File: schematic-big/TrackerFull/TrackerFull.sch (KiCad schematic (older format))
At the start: 50 parts, among them J1 SIM_Card, J2 Conn_01x05_Male, J7 Screw_Terminal_01x02, J8 USB_B_Mini, Q1 IRLML5203, Q2 IRLML0030, Q3 IRLML0030, U1 U.FL, U2 LIS3DSH, U3 MCP73831-2-OT, U4 LM350_TO220, U6 ATtiny85-20SU, U7 MCP1700-2502E_SOT23

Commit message: schematic fixes
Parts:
- R10, R11, R9: value 140 -> 125
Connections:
- wire segments 205 -> 203
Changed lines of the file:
@@
 P 2700 6150
 F 0 "R11" V 2630 6104 50  0000 R CNN
-F 1 "140" V 2600 6400 50  0000 R CNN
+F 1 "125" V 2600 6400 50  0000 R CNN
 F 2 "Resistor_SMD:R_0805_2012Metric_Pad1.15x1.40mm_HandSolder" H 2630 6241 50  0001 R CNN
 F 3 "~" H 2700 6150 50  0001 C CNN
@@
 P 2650 6350
 F 0 "R10" V 2580 6304 50  0000 R CNN
-F 1 "140" V 2550 6600 50  0000 R CNN
+F 1 "125" V 2550 6600 50  0000 R CNN
 F 2 "Resistor_SMD:R_0805_2012Metric_Pad1.15x1.40mm_HandSolder" H 2580 6441 50  0001 R CNN
 F 3 "~" H 2650 6350 50  0001 C CNN
@@
 P 2600 6550
 F 0 "R9" V 2530 6504 50  0000 R CNN
-F 1 "140" V 2450 6800 50  0000 R CNN
+F 1 "125" V 2450 6800 50  0000 R CNN
 F 2 "Resistor_SMD:R_0805_2012Metric_Pad1.15x1.40mm_HandSolder" H 2530 6641 50  0001 R CNN
 F 3 "~" H 2600 6550 50  0001 C CNN
@@
 Wire Wire Line
 	3050 6250 3450 6250
-Wire Wire Line
-	2950 6900 1800 6900
-Wire Wire Line
-	1800 6900 1800 6350
-Wire Wire Line
-	1800 6350 1950 6350
 $Comp
 L Regulator_Linear:MCP1700-2502E_SOT23 U7
@@
 Wire Wire Line
 	7600 5950 7750 5950
-Text Label 7850 5950 0    50   ~ 0
-2.2V
 Text Label 7000 7000 0    50   ~ 0
 2.2V
@@
 Wire Wire Line
 	6900 5950 7000 5950
-$Comp
-L Device:C C4
-U 1 1 5F5A6A6D
-P 7750 6100
-F 0 "C4" H 7865 6146 50  0000 L CNN
-F 1 "10uF" H 7865 6055 50  0000 L CNN
-F 2 "Capacitor_Tantalum_SMD:CP_EIA-3216-18_Kemet-A" H 7788 5950 50  0001 C CNN
-F 3 "~" H 7750 6100 50  0001 C CNN
-	1    7750 6100
-	1    0    0    -1
-$EndComp
 Connection ~ 7750 5950
 Wire Wire Line
@@
 	1    0    0    -1
 $EndComp
-Connection ~ 2950 6900
 $Comp
 L Transistor_FET:IRLML0030 Q3
@@
 	1    0    0    -1
 $EndComp
+$Comp
+L Device:C C4
+U 1 1 5F5A6A6D
+P 7750 6100
+F 0 "C4" H 7865 6146 50  0000 L CNN
+F 1 "10uF" H 7865 6055 50  0000 L CNN
+F 2 "Capacitor_Tantalum_SMD:CP_EIA-3216-18_Kemet-A" H 7788 5950 50  0001 C CNN
+F 3 "~" H 7750 6100 50  0001 C CNN
+	1    7750 6100
+	1    0    0    -1
+$EndComp
+Wire Wire Line
+	1500 6350 1950 6350
+Text Label 1500 6350 0    50   ~ 0
+2.2V
+Text Label 7850 5950 0    50   ~ 0
+2.2V
 $EndSCHEMATC

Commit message: schematic update
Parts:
- removed C14: 1uF, Capacitor_Tantalum_SMD:CP_EIA-3216-18_Kemet-A, symbol Device:C
- removed C3, C4: 10uF, Capacitor_Tantalum_SMD:CP_EIA-3216-18_Kemet-A, symbol Device:C
- removed LED1: TO-5050BC-MRPBFGF, LED_SMD:LED_RGB_5050-6, symbol Device:LED_RGB
- removed Q3: IRLML0030, Package_TO_SOT_SMD:SOT-23, symbol Transistor_FET:IRLML0030
- removed R10, R11: 125, Resistor_SMD:R_0805_2012Metric_Pad1.15x1.40mm_HandSolder, symbol Device:R
- removed R12: 100K, Resistor_SMD:R_0603_1608Metric, symbol Device:R
- removed U4: LM350_TO220, Package_TO_SOT_THT:TO-220-3_Horizontal_TabDown, symbol Regulator_Linear:LM350_TO220
- removed U7: MCP1700-2502E_SOT23, Package_TO_SOT_SMD:SOT-23, symbol Regulator_Linear:MCP1700-2502E_SOT23
- added C15: 10uF, Capacitor_Tantalum_SMD:CP_EIA-3216-18_Kemet-A, symbol Device:C
- added C18: 10uF, Capacitor_SMD:C_1206_3216Metric_Pad1.42x1.75mm_HandSolder, symbol Device:C
- added C19: 22uF, Capacitor_Tantalum_SMD:CP_EIA-3216-18_Kemet-A, symbol Device:C
- added C20: 4.7u, Capacitor_SMD:C_1206_3216Metric_Pad1.42x1.75mm_HandSolder, symbol Device:C
- added D3: SK6812, LED_SMD:LED_SK6812_PLCC4_5.0x5.0mm_P3.2mm, symbol LED:SK6812
- added L2: SRR0604-3R3ML, Inductor_THT:L_Radial_D8.7mm_P5.00mm_Fastron_07HCP, symbol mailboxNotifier-eagle-import:INDUCTOR
- added R14: 10K, Resistor_SMD:R_0805_2012Metric_Pad1.15x1.40mm_HandSolder, symbol Device:R
- added U5: LP2985-3.3, Package_TO_SOT_SMD:SOT-23-5, symbol Regulator_Linear:LP2985-3.3
- C12: renamed from C11; footprint Capacitor_Tantalum_SMD:CP_EIA-3216-18_Kemet-A -> Capacitor_SMD:C_1206_3216Metric_Pad1.42x1.75mm_HandSolder
- C13: renamed from C12; footprint Capacitor_Tantalum_SMD:CP_EIA-3216-18_Kemet-A -> Capacitor_SMD:C_1206_3216Metric_Pad1.42x1.75mm_HandSolder
- C14: renamed from C13; footprint Capacitor_Tantalum_SMD:CP_EIA-3216-18_Kemet-A -> Capacitor_SMD:C_1206_3216Metric_Pad1.42x1.75mm_HandSolder
- C8: footprint Capacitor_Tantalum_SMD:CP_EIA-3216-18_Kemet-A -> Capacitor_SMD:C_1206_3216Metric_Pad1.42x1.75mm_HandSolder
- D2: footprint Package_SO:SOP-8_3.76x4.96mm_P1.27mm -> Package_SO:SOP-8_3.9x4.9mm_P1.27mm
- J1: footprint Connector_Card:microSIM_JAE_SF53S006VCBR2000 -> mailboxNotifier:SIM_SOCKET1
- R2: value 47000 -> 43000
- R9: value 125 -> 10000; footprint Resistor_SMD:R_0805_2012Metric_Pad1.15x1.40mm_HandSolder -> Resistor_SMD:R_0603_1608Metric
- renumbered C15 to C21
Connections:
- net labels added: ACCEL_INT2, IO8, IO9, LED_CTL
- net labels removed: 2.2V, GPS_CTRL
- wire segments 203 -> 201
- no-connect marks 5 -> 6
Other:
- moved on the sheet: D1, J2

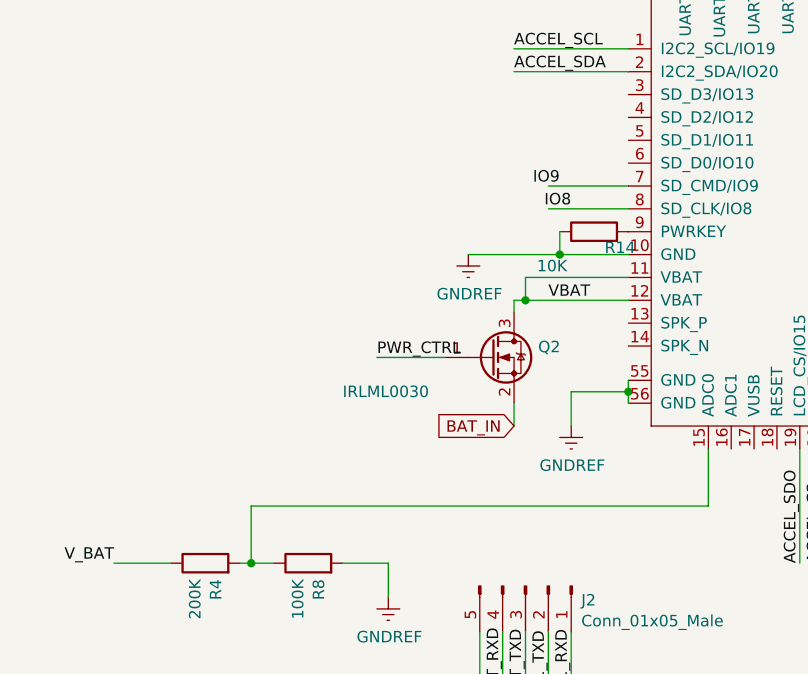
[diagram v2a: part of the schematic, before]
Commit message: schematic update
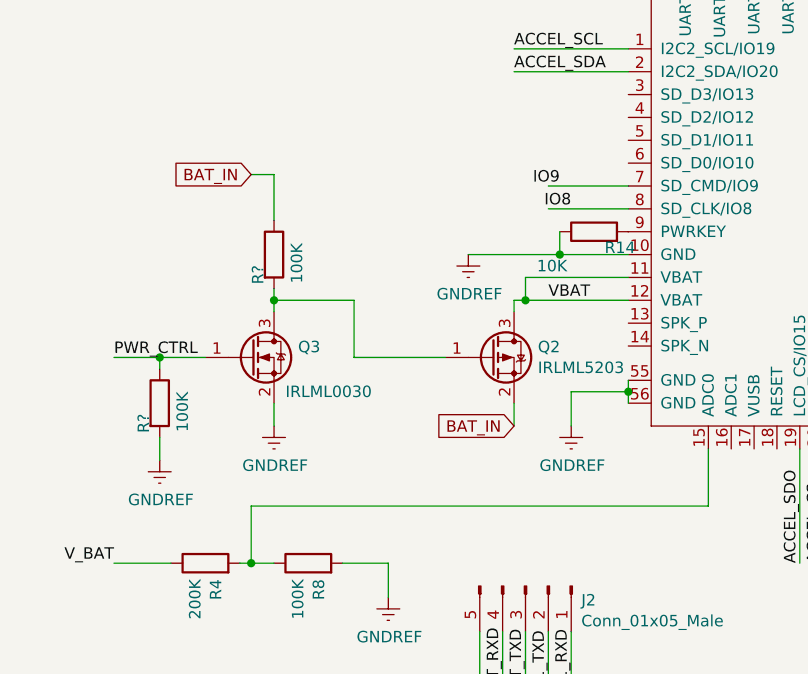
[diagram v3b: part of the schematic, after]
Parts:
- added Q2: IRLML5203, Package_TO_SOT_SMD:SOT-23, symbol Transistor_FET:IRLML5203
- added R? (x2): 100K, Resistor_SMD:R_0805_2012Metric_Pad1.15x1.40mm_HandSolder, symbol Device:R
- renumbered Q2 to Q3
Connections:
- wire segments 201 -> 212
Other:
- moved on the sheet: Q3
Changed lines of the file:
@@
 Wire Wire Line
 	2950 7300 2950 7400
-Text Label 2350 7100 0    50   ~ 0
+Text Label 1200 7100 0    50   ~ 0
 PWR_CTRL
 $Comp
@@
 	1    0    0    -1
 $EndComp
-Wire Wire Line
-	2350 7100 2650 7100
 Wire Wire Line
 	3000 6850 3450 6850
@@
 VBAT
 $Comp
-L Transistor_FET:IRLML0030 Q2
+L Transistor_FET:IRLML0030 Q3
 U 1 1 5F6E0FC1
-P 2850 7100
-F 0 "Q2" H 3055 7146 50  0000 L CNN
-F 1 "IRLML0030" H 2200 6950 50  0000 L CNN
-F 2 "Package_TO_SOT_SMD:SOT-23" H 3050 7025 50  0001 L CIN
-F 3 "https://www.infineon.com/dgdl/irlml0030pbf.pdf?fileId=5546d462533600a401535664773825df" H 2850 7100 50  0001 L CNN
-	1    2850 7100
+P 1800 7100
+F 0 "Q3" H 2005 7146 50  0000 L CNN
+F 1 "IRLML0030" H 1950 6950 50  0000 L CNN
+F 2 "Package_TO_SOT_SMD:SOT-23" H 2000 7025 50  0001 L CIN
+F 3 "https://www.infineon.com/dgdl/irlml0030pbf.pdf?fileId=5546d462533600a401535664773825df" H 1800 7100 50  0001 L CNN
+	1    1800 7100
 	1    0    0    -1
 $EndComp
@@
 	11700 4150 14150 4150
 Connection ~ 14150 4150
+$Comp
+L Transistor_FET:IRLML5203 Q2
+U 1 1 5F66A3D8
+P 2850 7100
+F 0 "Q2" H 3054 7146 50  0000 L CNN
+F 1 "IRLML5203" H 3054 7055 50  0000 L CNN
+F 2 "Package_TO_SOT_SMD:SOT-23" H 3050 7025 50  0001 L CIN
+F 3 "https://www.infineon.com/dgdl/irlml5203pbf.pdf?fileId=5546d462533600a40153566868da261d" H 2850 7100 50  0001 L CNN
+	1    2850 7100
+	1    0    0    -1
+$EndComp
+Wire Wire Line
+	2250 7100 2650 7100
+Wire Wire Line
+	1600 7100 1400 7100
+Wire Wire Line
+	1900 7300 1900 7400
+$Comp
+L power:GNDREF #PWR0132
+U 1 1 5F6ADE8F
+P 1900 7400
+F 0 "#PWR0132" H 1900 7150 50  0001 C CNN
+F 1 "GNDREF" H 1905 7227 50  0000 C CNN
+F 2 "" H 1900 7400 50  0001 C CNN
+F 3 "" H 1900 7400 50  0001 C CNN
+	1    1900 7400
+	1    0    0    -1
+$EndComp
+Text GLabel 1800 6300 0    50   Input ~ 0
+BAT_IN
+$Comp
+L Device:R R?
+U 1 1 5F6F9FFF
+P 1900 6650
+F 0 "R?" V 1830 6604 50  0000 R CNN
+F 1 "100K" V 2000 6700 50  0000 R CNN
+F 2 "Resistor_SMD:R_0805_2012Metric_Pad1.15x1.40mm_HandSolder" H 1830 6741 50  0001 R CNN
+F 3 "~" H 1900 6650 50  0001 C CNN
+	1    1900 6650
+	1    0    0    -1
+$EndComp
+Wire Wire Line
+	1900 6900 1900 6850
+Wire Wire Line
+	1900 6850 2250 6850
+Connection ~ 1900 6850
+Wire Wire Line
+	1900 6850 1900 6800
+Wire Wire Line
+	1900 6300 1800 6300
+Wire Wire Line
+	1900 6300 1900 6500
+Wire Wire Line
+	2250 7100 2250 6850
+$Comp
+L Device:R R?
+U 1 1 5F753720
+P 1400 7300
+F 0 "R?" V 1330 7254 50  0000 R CNN
+F 1 "100K" V 1500 7350 50  0000 R CNN
+F 2 "Resistor_SMD:R_0805_2012Metric_Pad1.15x1.40mm_HandSolder" H 1330 7391 50  0001 R CNN
+F 3 "~" H 1400 7300 50  0001 C CNN
+	1    1400 7300
+	1    0    0    -1
+$EndComp
+Wire Wire Line
+	1400 7100 1400 7150
+Connection ~ 1400 7100
+Wire Wire Line
+	1400 7100 1200 7100
+Wire Wire Line
+	1400 7450 1400 7550
+$Comp
+L power:GNDREF #PWR?
+U 1 1 5F7617DA
+P 1400 7550
+F 0 "#PWR?" H 1400 7300 50  0001 C CNN
+F 1 "GNDREF" H 1405 7377 50  0000 C CNN
+F 2 "" H 1400 7550 50  0001 C CNN
+F 3 "" H 1400 7550 50  0001 C CNN
+	1    1400 7550
+	1    0    0    -1
+$EndComp
 $EndSCHEMATC

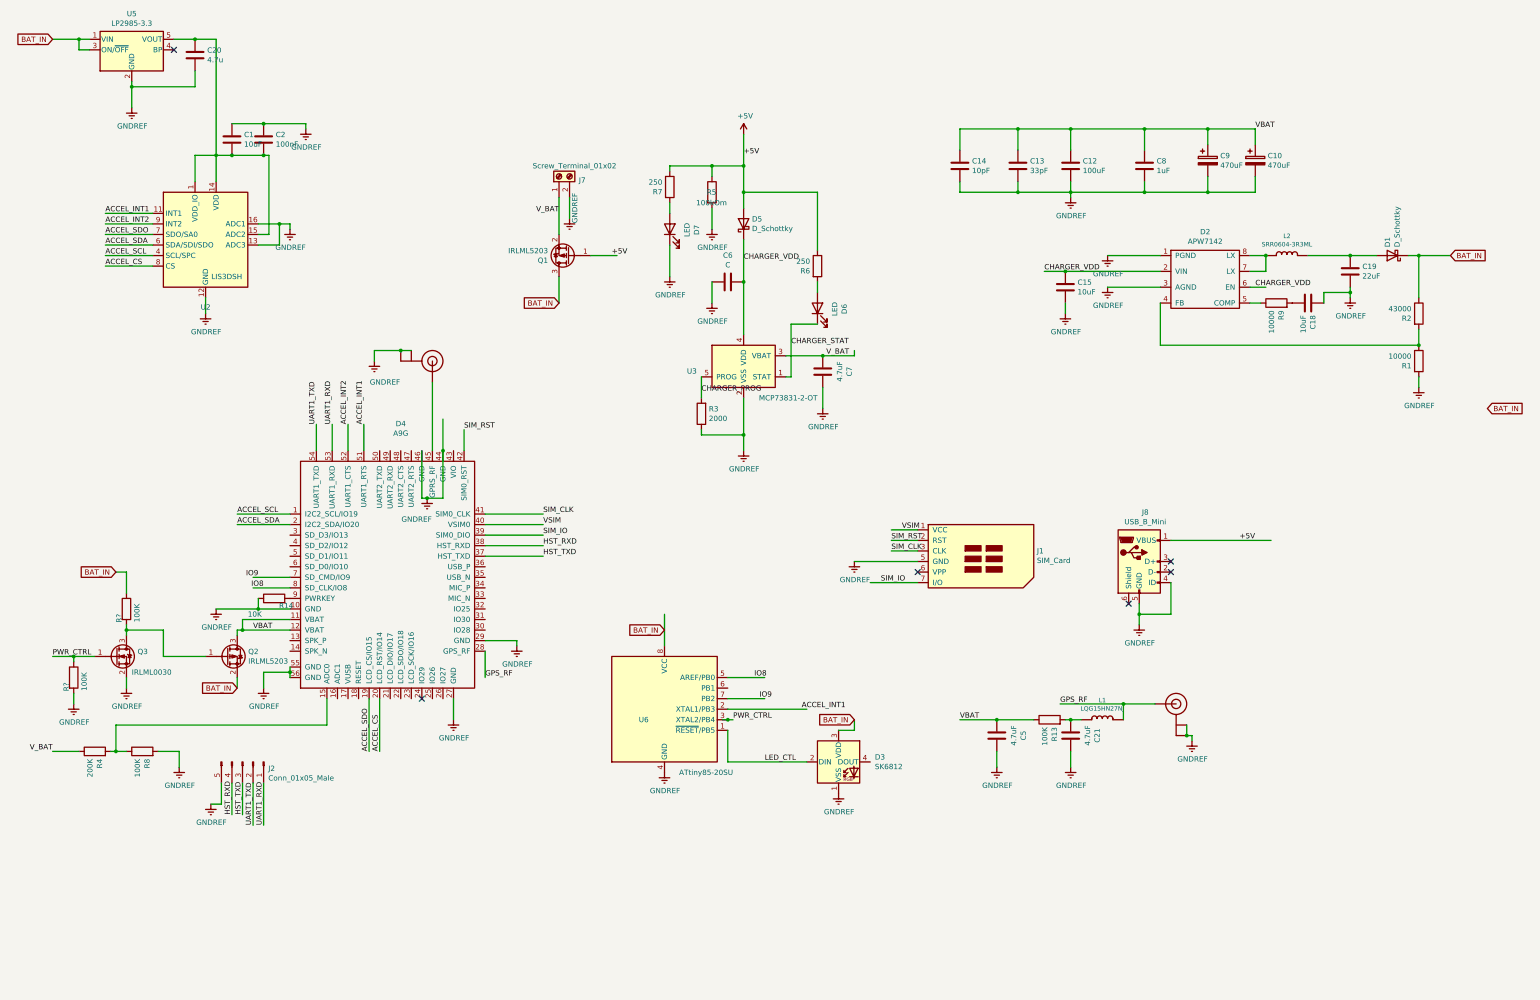
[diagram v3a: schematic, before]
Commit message: schematic update
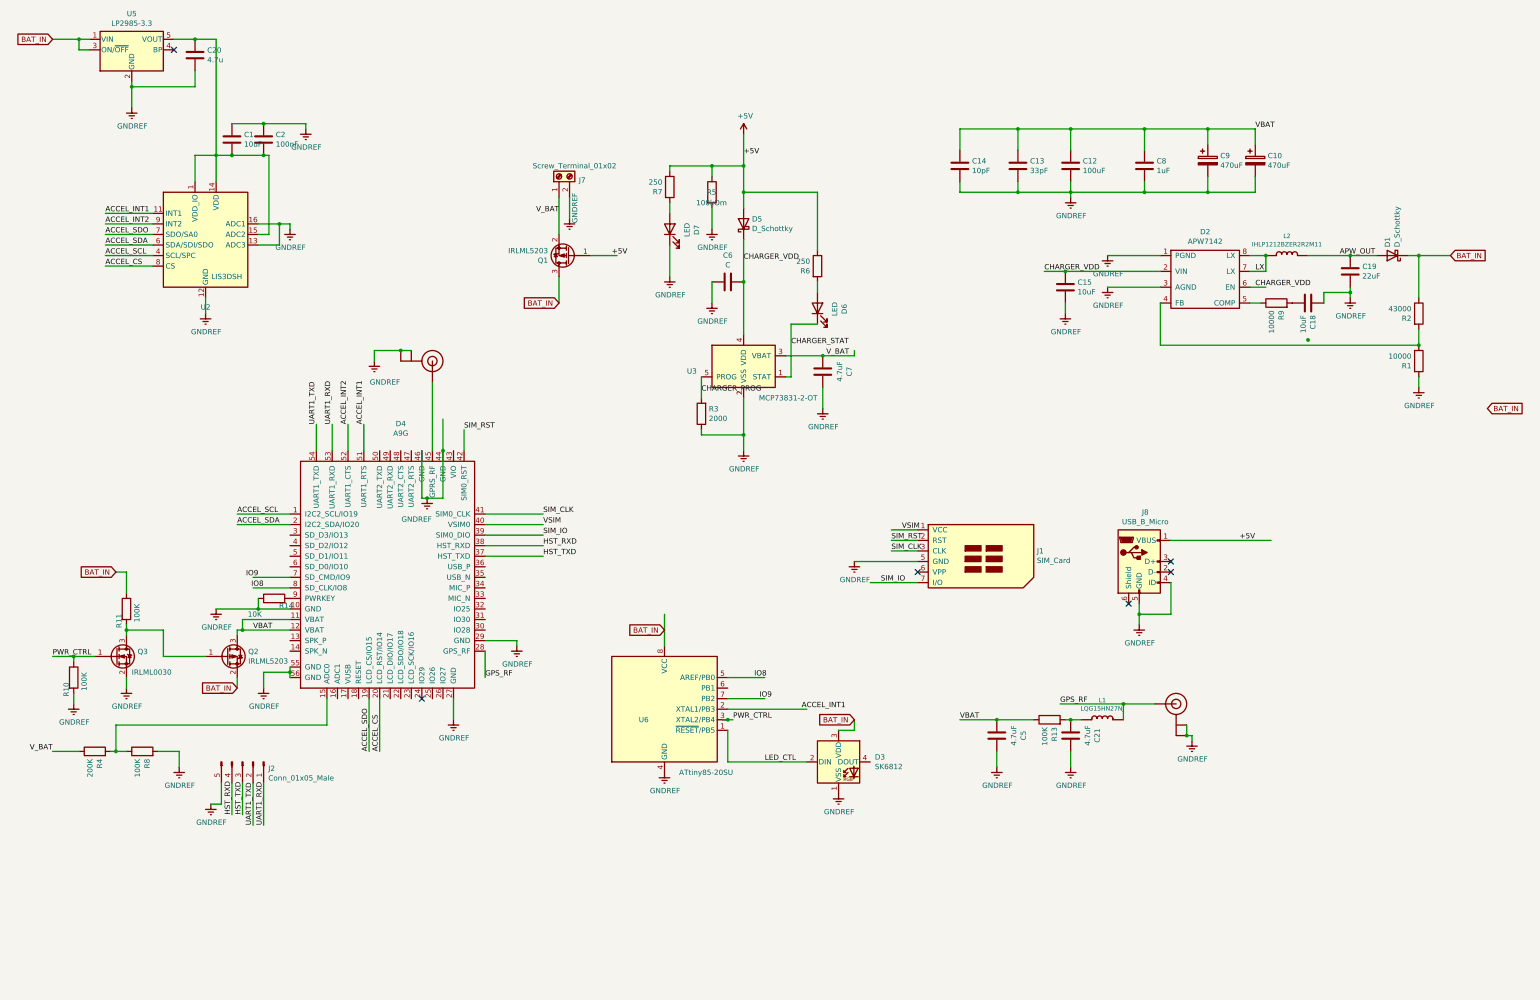
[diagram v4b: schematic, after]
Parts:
- removed J8: USB_B_Mini, Connector_USB:USB_Micro-B_Molex-105017-0001, symbol Connector:USB_B_Mini
- removed L2: SRR0604-3R3ML, Inductor_THT:L_Radial_D8.7mm_P5.00mm_Fastron_07HCP, symbol mailboxNotifier-eagle-import:INDUCTOR
- added J8: USB_B_Micro, Connector_USB:USB_Micro-B_Molex-105017-0001, symbol Connector:USB_B_Micro
- added L2: IHLP1212BZER2R2M11, Inductor_SMD:L_Vishay_IHLP-1212, symbol mailboxNotifier-eagle-import:INDUCTOR1210K
- gave numbers to parts that had none: 2
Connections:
- net labels added: APW_OUT, LX
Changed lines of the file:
@@
 BAT_IN
-$Comp
-L Connector:USB_B_Mini J8
-U 1 1 5F3D5D9C
-P 11500 6200
-F 0 "J8" H 11557 6667 50  0000 C CNN
-F 1 "USB_B_Mini" H 11557 6576 50  0000 C CNN
-F 2 "Connector_USB:USB_Micro-B_Molex-105017-0001" H 11650 6150 50  0001 C CNN
-F 3 "~" H 11650 6150 50  0001 C CNN
-	1    11500 6200
-	1    0    0    -1
-$EndComp
 $Comp
 L power:GNDREF #PWR0123
@@
 	4150 5150 4150 4900
 $Comp
-L mailboxNotifier-eagle-import:INDUCTOR L2
-U 1 1 5F86E20B
-P 12900 3300
-F 0 "L2" H 12900 3485 42  0000 C CNN
-F 1 "SRR0604-3R3ML" H 12900 3406 42  0000 C CNN
-F 2 "Inductor_THT:L_Radial_D8.7mm_P5.00mm_Fastron_07HCP" H 12900 3300 50  0001 C CNN
-F 3 "" H 12900 3300 50  0001 C CNN
-	1    12900 3300
-	1    0    0    -1
-$EndComp
-$Comp
 L Device:R R1
 U 1 1 5F8B8213
@@
 BAT_IN
 $Comp
-L Device:R R?
+L Device:R R11
 U 1 1 5F6F9FFF
 P 1900 6650
-F 0 "R?" V 1830 6604 50  0000 R CNN
+F 0 "R11" V 1830 6604 50  0000 R CNN
 F 1 "100K" V 2000 6700 50  0000 R CNN
 F 2 "Resistor_SMD:R_0805_2012Metric_Pad1.15x1.40mm_HandSolder" H 1830 6741 50  0001 R CNN
@@
 	2250 7100 2250 6850
 $Comp
-L Device:R R?
+L Device:R R10
 U 1 1 5F753720
 P 1400 7300
-F 0 "R?" V 1330 7254 50  0000 R CNN
+F 0 "R10" V 1330 7254 50  0000 R CNN
 F 1 "100K" V 1500 7350 50  0000 R CNN
 F 2 "Resistor_SMD:R_0805_2012Metric_Pad1.15x1.40mm_HandSolder" H 1330 7391 50  0001 R CNN
@@
 	1400 7450 1400 7550
 $Comp
-L power:GNDREF #PWR?
+L power:GNDREF #PWR0133
 U 1 1 5F7617DA
 P 1400 7550
-F 0 "#PWR?" H 1400 7300 50  0001 C CNN
+F 0 "#PWR0133" H 1400 7300 50  0001 C CNN
 F 1 "GNDREF" H 1405 7377 50  0000 C CNN
 F 2 "" H 1400 7550 50  0001 C CNN
@@
 	1    0    0    -1
 $EndComp
+$Comp
+L mailboxNotifier-eagle-import:INDUCTOR1210K L2
+U 1 1 5F68883E
+P 12900 3300
+F 0 "L2" H 12900 3485 42  0000 C CNN
+F 1 "IHLP1212BZER2R2M11" H 12900 3406 42  0000 C CNN
+F 2 "Inductor_SMD:L_Vishay_IHLP-1212" H 12900 3300 50  0001 C CNN
+F 3 "" H 12900 3300 50  0001 C CNN
+	1    12900 3300
+	1    0    0    -1
+$EndComp
+Text Label 12600 3450 0    50   ~ 0
+LX
+Text Label 13400 3300 0    50   ~ 0
+APW_OUT
+$Comp
+L Connector:USB_B_Micro J8
+U 1 1 5F6BD00D
+P 11500 6200
+F 0 "J8" H 11557 6667 50  0000 C CNN
+F 1 "USB_B_Micro" H 11557 6576 50  0000 C CNN
+F 2 "Connector_USB:USB_Micro-B_Molex-105017-0001" H 11650 6150 50  0001 C CNN
+F 3 "http://www.farnell.com/datasheets/2693980.pdf" H 11650 6150 50  0001 C CNN
+	1    11500 6200
+	1    0    0    -1
+$EndComp
+Connection ~ 13100 4100
 $EndSCHEMATC
